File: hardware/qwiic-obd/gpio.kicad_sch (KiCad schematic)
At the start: 24 parts, among them SW401 SW_Push, U401 TCA9534, U402 MCP3423, U403 TCA9534, U404 ADM6320BX33ARJZ-R7, U405 TCA9534

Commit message: Added initial layout (parts dump)
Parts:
- C402: value 100uF 6V3 -> 10uF 6V3; footprint (none) -> Capacitor_SMD:C_0805_2012Metric_Pad1.18x1.45mm_HandSolder
- D401, D403: footprint Diode_SMD:D_0402_1005Metric_Pad0.77x0.64mm_HandSolder -> Diode_SMD:D_SOD-523
- R409: footprint (none) -> Resistor_SMD:R_0805_2012Metric_Pad1.20x1.40mm_HandSolder
- RN401, RN402, RN403: footprint Package_SO:SOIC-16_3.9x9.9mm_P1.27mm -> UltraLibrarian:742C163103JP
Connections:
- net +3V3_NOSW: now also RN402.7 (R7.1)
- net CAN_SOF: now also RN402.9 (R8.2), U403.12 (P7); no longer RN402.10 (R7.2), U403.11 (P6)
- net GND: no longer RN402.7 (R7.1)
- net ~{CAN_RESET}: no longer names the net of RN402.11 (R6.2), U403.10 (P5)
- new net: RN402.10 (R7.2), U403.11 (P6)
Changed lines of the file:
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@@
   (junction (at 106.68 48.26) (diameter 0) (color 0 0 0 0)
   )
-  (junction (at 106.68 115.57) (diameter 0) (color 0 0 0 0)
-  )
   (junction (at 96.52 83.82) (diameter 0) (color 0 0 0 0)
   )
@@
   (junction (at 99.06 107.95) (diameter 0) (color 0 0 0 0)
   )
+  (junction (at 109.22 118.11) (diameter 0) (color 0 0 0 0)
+  )
   (junction (at 101.6 67.31) (diameter 0) (color 0 0 0 0)
   )
@@
   (junction (at 62.23 173.99) (diameter 0) (color 0 0 0 0)
   )
+  (junction (at 104.14 83.82) (diameter 0) (color 0 0 0 0)
+  )
   (junction (at 148.59 83.82) (diameter 0) (color 0 0 0 0)
   )
@@
   (junction (at 74.93 59.69) (diameter 0) (color 0 0 0 0)
   )
-  (junction (at 104.14 113.03) (diameter 0) (color 0 0 0 0)
-  )
   (junction (at 101.6 83.82) (diameter 0) (color 0 0 0 0)
   )
@@
   )
   (junction (at 109.22 67.31) (diameter 0) (color 0 0 0 0)
-  )
-  (junction (at 109.22 81.28) (diameter 0) (color 0 0 0 0)
   )
   (junction (at 55.88 142.24) (diameter 0) (color 0 0 0 0)
@@
     (stroke (width 0) (type default) (color 0 0 0 0))
   )
-  (wire (pts (xy 106.68 115.57) (xy 111.76 115.57))
-    (stroke (width 0) (type default) (color 0 0 0 0))
-  )
   (wire (pts (xy 106.68 139.7) (xy 109.22 139.7))
     (stroke (width 0) (type default) (color 0 0 0 0))
@@
     (stroke (width 0) (type default) (color 0 0 0 0))
   )
-  (wire (pts (xy 106.68 81.28) (xy 109.22 81.28))
-    (stroke (width 0) (type default) (color 0 0 0 0))
-  )
   (wire (pts (xy 63.5 142.24) (xy 63.5 171.45))
     (stroke (width 0) (type default) (color 0 0 0 0))
@@
     (stroke (width 0) (type default) (color 0 0 0 0))
   )
+  (wire (pts (xy 106.68 83.82) (xy 104.14 83.82))
+    (stroke (width 0) (type default) (color 0 0 0 0))
+  )
   (wire (pts (xy 55.88 142.24) (xy 63.5 142.24))
     (stroke (width 0) (type default) (color 0 0 0 0))
@@
     (stroke (width 0) (type default) (color 0 0 0 0))
   )
+  (wire (pts (xy 109.22 118.11) (xy 111.76 118.11))
+    (stroke (width 0) (type default) (color 0 0 0 0))
+  )
   (wire (pts (xy 104.14 139.7) (xy 104.14 143.51))
     (stroke (width 0) (type default) (color 0 0 0 0))
@@
     (stroke (width 0) (type default) (color 0 0 0 0))
   )
+  (wire (pts (xy 106.68 87.63) (xy 106.68 83.82))
+    (stroke (width 0) (type default) (color 0 0 0 0))
+  )
   (wire (pts (xy 205.74 64.77) (xy 220.98 64.77))
     (stroke (width 0) (type default) (color 0 0 0 0))
@@
     (stroke (width 0) (type default) (color 0 0 0 0))
   )
-  (wire (pts (xy 104.14 113.03) (xy 111.76 113.03))
-    (stroke (width 0) (type default) (color 0 0 0 0))
-  )
   (wire (pts (xy 186.69 132.08) (xy 190.5 132.08))
     (stroke (width 0) (type default) (color 0 0 0 0))
@@
   )
   (wire (pts (xy 109.22 67.31) (xy 109.22 71.12))
-    (stroke (width 0) (type default) (color 0 0 0 0))
-  )
-  (wire (pts (xy 106.68 87.63) (xy 106.68 81.28))
     (stroke (width 0) (type default) (color 0 0 0 0))
   )
@@
     )
   )
-  (global_label "CAN_SOF" (shape input) (at 111.76 115.57 0) (fields_autoplaced)
+  (global_label "CAN_SOF" (shape input) (at 111.76 118.11 0) (fields_autoplaced)
     (effects (font (size 1.27 1.27)) (justify left))
-    (property "Intersheet References" "${INTERSHEET_REFS}" (id 0) (at 122.4583 115.4906 0)
+    (property "Intersheet References" "${INTERSHEET_REFS}" (id 0) (at 122.4583 118.0306 0)
       (effects (font (size 1.27 1.27)) (justify left) hide)
     )
@@
     (property "Intersheet References" "${INTERSHEET_REFS}" (id 0) (at 126.4734 43.1118 0)
       (effects (font (size 1.0922 1.0922)) (justify left) hide)
-    )
-  )
-  (global_label "~{CAN_RESET}" (shape output) (at 111.76 113.03 0) (fields_autoplaced)
-    (effects (font (size 1.27 1.27)) (justify left))
-    (property "Intersheet References" "${INTERSHEET_REFS}" (id 0) (at 124.575 112.9506 0)
-      (effects (font (size 1.27 1.27)) (justify left) hide)
     )
   )
@@
       (effects (font (size 1.27 1.27)) (justify left))
     )
-    (property "Footprint" "Package_SO:SOIC-16_3.9x9.9mm_P1.27mm" (id 2) (at 113.665 92.71 90)
+    (property "Footprint" "UltraLibrarian:742C163103JP" (id 2) (at 113.665 92.71 90)
       (effects (font (size 1.27 1.27)) hide)
     )
@@
       (effects (font (size 1.27 1.27)) (justify left))
     )
-    (property "Footprint" "Diode_SMD:D_0402_1005Metric_Pad0.77x0.64mm_HandSolder" (id 2) (at 180.34 52.07 0)
+    (property "Footprint" "Diode_SMD:D_SOD-523" (id 2) (at 180.34 52.07 0)
       (effects (font (size 1.27 1.27)) hide)
     )
@@
       (effects (font (size 1.27 1.27)) (justify left))
     )
-    (property "Footprint" "Package_SO:SOIC-16_3.9x9.9mm_P1.27mm" (id 2) (at 113.665 58.42 90)
+    (property "Footprint" "UltraLibrarian:742C163103JP" (id 2) (at 113.665 58.42 90)
       (effects (font (size 1.27 1.27)) hide)
     )
@@
       (effects (font (size 1.27 1.27)) (justify left))
     )
-    (property "Footprint" "" (id 2) (at 54.102 149.86 90)
+    (property "Footprint" "Resistor_SMD:R_0805_2012Metric_Pad1.20x1.40mm_HandSolder" (id 2) (at 54.102 149.86 90)
       (effects (font (size 1.27 1.27)) hide)
     )
@@
       (effects (font (size 1.27 1.27)) (justify left))
     )
-    (property "Footprint" "Diode_SMD:D_0402_1005Metric_Pad0.77x0.64mm_HandSolder" (id 2) (at 179.07 88.9 0)
+    (property "Footprint" "Diode_SMD:D_SOD-523" (id 2) (at 179.07 88.9 0)
       (effects (font (size 1.27 1.27)) hide)
     )
@@
       (effects (font (size 1.27 1.27)) (justify right))
     )
-    (property "Value" "100uF 6V3" (id 1) (at 138.43 90.1699 0)
+    (property "Value" "10uF 6V3" (id 1) (at 138.43 90.1699 0)
       (effects (font (size 1.27 1.27)) (justify right))
     )
-    (property "Footprint" "" (id 2) (at 143.2052 85.09 0)
+    (property "Footprint" "Capacitor_SMD:C_0805_2012Metric_Pad1.18x1.45mm_HandSolder" (id 2) (at 143.2052 85.09 0)
       (effects (font (size 1.27 1.27)) hide)
     )
@@
       (effects (font (size 1.27 1.27)) (justify left))
     )
-    (property "Footprint" "Package_SO:SOIC-16_3.9x9.9mm_P1.27mm" (id 2) (at 113.665 148.59 90)
-      (effects (font (size 1.27 1.27)) hide)
-    )
+    (property "Footprint" "UltraLibrarian:742C163103JP" (id 2) (at 113.665 148.59 90)
+      (effects (font (size 1.27 1.27)) hide)
+    )

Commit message: OK, layout v1 complete
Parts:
- removed R409: 10k, Resistor_SMD:R_0805_2012Metric_Pad1.20x1.40mm_HandSolder, symbol Device:R
- removed RN403: 10k, UltraLibrarian:742C163103JP, symbol Device:R_Pack08
- removed U405: TCA9534, Package_SO:TSSOP-16_4.4x5mm_P0.65mm, symbol Interface_Expansion:TCA9534
- added J401: 1x4, Connector_PinSocket_2.54mm:PinSocket_1x04_P2.54mm_Vertical, symbol SparkFun-Connectors:M04JST-PTH
- added RN403: 10k, Resistor_THT:R_Array_SIP5, symbol Device:R_Network04
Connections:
- net +3V3_NOSW: now also RN402.10 (R7.2), RN402.11 (R6.2), RN402.12 (R5.2), RN402.13 (R4.2), RN402.14 (R3.2), RN402.15 (R2.2), RN402.16 (R1.2), RN403.1 (common); no longer RN402.1 (R1.1), RN402.2 (R2.1), RN402.3 (R3.1), RN402.4 (R4.1), RN402.5 (R5.1), RN402.6 (R6.1), RN402.7 (R7.1)
- net CAN_SOF: now also RN402.8 (R8.1); no longer RN402.9 (R8.2)
- net GND: now also RN402.9 (R8.2); no longer RN402.8 (R8.1)
- net ~{CAN_INT}: now also J401.1, RN403.2 (R1)
- net ~{CAN_RX0BF}: now also RN402.1 (R1.1); no longer RN402.16 (R1.2)
- net ~{CAN_RX1BF}: now also RN402.2 (R2.1); no longer RN402.15 (R2.2)
- net ~{CAN_TX0RTS}: now also RN402.3 (R3.1); no longer RN402.14 (R3.2)
- net ~{CAN_TX1RTS}: now also RN402.4 (R4.1); no longer RN402.13 (R4.2)
- net ~{CAN_TX2RTS}: now also RN402.5 (R5.1); no longer RN402.12 (R5.2)
- net ~{J1850_INT}: now also J401.4, RN403.5 (R4)
- net ~{RESET}: now also RN402.7 (R7.1), U403.11 (P6)
- net ~{SPI_INT}: now also J401.3, RN403.4 (R3)
- net ~{UART_INT}: now also J401.2, RN403.3 (R2)
- net at U403.10 (P5): now also RN402.6 (R6.1); no longer RN402.11 (R6.2)
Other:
- note removed: "I2C Address 0x22"
- moved on the sheet: RN402

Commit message: Fix title block
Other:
- title: (none) -> QWIIC OBDII Interface
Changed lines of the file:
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@@
 (kicad_sch (version 20211123) (generator eeschema)
   (paper "A4")
+  (title_block
+    (title "QWIIC OBDII Interface")
+    (date "2023-01-03")
+  )
   (junction (at 236.22 76.2) (diameter 0) (color 0 0 0 0)
   )

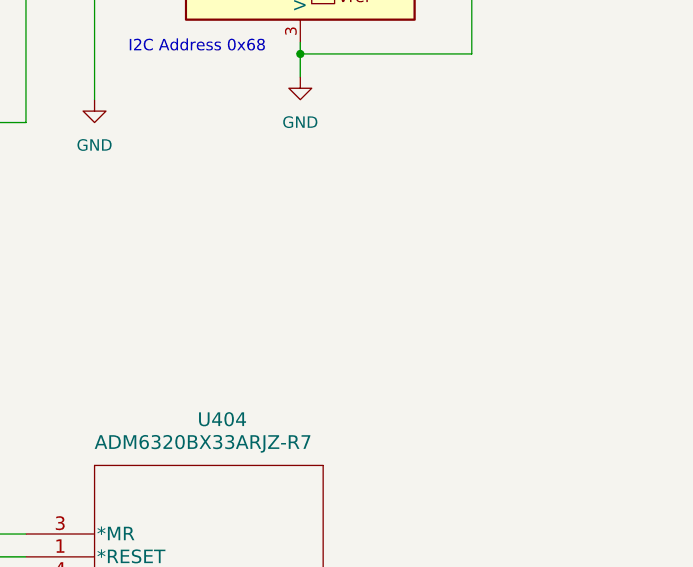
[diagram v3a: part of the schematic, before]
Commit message: Add PIC bootloader, update silkscreen
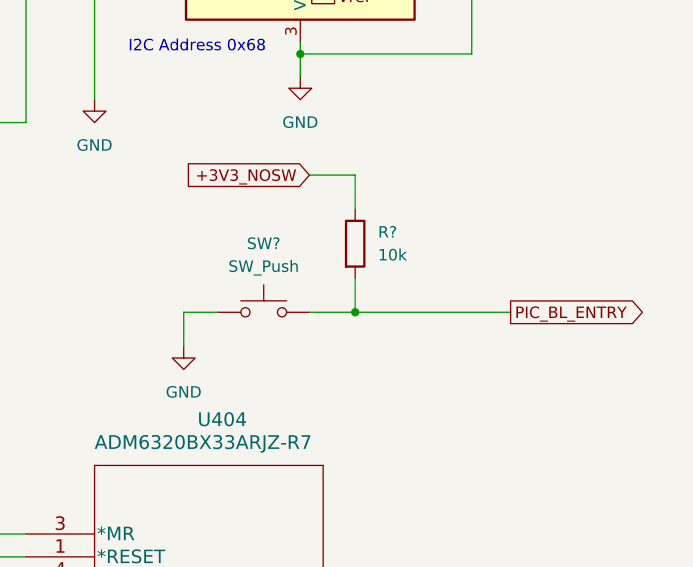
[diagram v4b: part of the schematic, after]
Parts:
- added R?: 10k, Resistor_SMD:R_0805_2012Metric_Pad1.20x1.40mm_HandSolder, symbol Device:R
- added SW?: SW_Push, Button_Switch_THT:SW_PUSH_6mm, symbol Switch:SW_Push
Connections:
- net +3V3_NOSW: now also R?.1
- net GND: now also SW?.1
- new net PIC_BL_ENTRY: R?.2, SW?.2
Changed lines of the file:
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@@
   (junction (at 167.64 46.99) (diameter 0) (color 0 0 0 0)
+  )
+  (junction (at 242.316 104.902) (diameter 0) (color 0 0 0 0)
   )
   (junction (at 101.6 137.16) (diameter 0) (color 0 0 0 0)
@@
     (stroke (width 0) (type default) (color 0 0 0 0))
   )
+  (wire (pts (xy 223.266 108.712) (xy 223.266 104.902))
+    (stroke (width 0) (type default) (color 0 0 0 0))
+  )
   (wire (pts (xy 109.22 132.08) (xy 109.22 137.16))
     (stroke (width 0) (type default) (color 0 0 0 0))
@@
     (stroke (width 0) (type default) (color 0 0 0 0))
   )
+  (wire (pts (xy 223.266 104.902) (xy 227.076 104.902))
+    (stroke (width 0) (type default) (color 0 0 0 0))
+  )
   (wire (pts (xy 93.98 67.31) (xy 96.52 67.31))
     (stroke (width 0) (type default) (color 0 0 0 0))
@@
     (stroke (width 0) (type default) (color 0 0 0 0))
   )
+  (wire (pts (xy 242.316 104.902) (xy 259.588 104.902))
+    (stroke (width 0) (type default) (color 0 0 0 0))
+  )
   (wire (pts (xy 255.27 67.31) (xy 255.27 76.2))
     (stroke (width 0) (type default) (color 0 0 0 0))
@@
     (stroke (width 0) (type default) (color 0 0 0 0))
   )
+  (wire (pts (xy 242.316 89.662) (xy 242.316 93.472))
+    (stroke (width 0) (type default) (color 0 0 0 0))
+  )
   (wire (pts (xy 106.68 115.57) (xy 111.76 115.57))
     (stroke (width 0) (type default) (color 0 0 0 0))
@@
     (stroke (width 0) (type default) (color 0 0 0 0))
   )
+  (wire (pts (xy 237.236 89.662) (xy 242.316 89.662))
+    (stroke (width 0) (type default) (color 0 0 0 0))
+  )
   (wire (pts (xy 109.22 63.5) (xy 109.22 67.31))
     (stroke (width 0) (type default) (color 0 0 0 0))
@@
     (stroke (width 0) (type default) (color 0 0 0 0))
   )
+  (wire (pts (xy 242.316 104.902) (xy 242.316 101.092))
+    (stroke (width 0) (type default) (color 0 0 0 0))
+  )
   (wire (pts (xy 167.64 44.704) (xy 167.64 46.99))
     (stroke (width 0) (type default) (color 0 0 0 0))
@@
   )
   (wire (pts (xy 85.09 50.8) (xy 109.22 50.8))
+    (stroke (width 0) (type default) (color 0 0 0 0))
+  )
+  (wire (pts (xy 237.236 104.902) (xy 242.316 104.902))
     (stroke (width 0) (type default) (color 0 0 0 0))
   )
@@
     )
   )
+  (global_label "PIC_BL_ENTRY" (shape output) (at 259.588 104.902 0) (fields_autoplaced)
+    (effects (font (size 1.27 1.27)) (justify left))
+    (property "Intersheet References" "${INTERSHEET_REFS}" (id 0) (at 275.1849 104.8226 0)
+      (effects (font (size 1.27 1.27)) (justify left) hide)
+    )
+  )
   (global_label "CAN_SEL0" (shape output) (at 111.76 50.8 0) (fields_autoplaced)
     (effects (font (size 1.27 1.27)) (justify left))
     (property "Intersheet References" "${INTERSHEET_REFS}" (id 0) (at 123.426 50.7206 0)
       (effects (font (size 1.27 1.27)) (justify left) hide)
+    )
+  )
+  (global_label "+3V3_NOSW" (shape input) (at 237.236 89.662 180) (fields_autoplaced)
+    (effects (font (size 1.27 1.27)) (justify right))
+    (property "Intersheet References" "${INTERSHEET_REFS}" (id 0) (at 223.4534 89.5826 0)
+      (effects (font (size 1.27 1.27)) (justify right) hide)
     )
   )
@@
     (pin "2")
   )
+  (symbol (lib_id "power:GND") (at 223.266 108.712 0) (unit 1)
+    (in_bom yes) (on_board yes) (fields_autoplaced)
+    (property "Reference" "#PWR?" (id 0) (at 223.266 115.062 0)
+      (effects (font (size 1.27 1.27)) hide)
+    )
+    (property "Value" "GND" (id 1) (at 223.266 113.792 0))
+    (property "Footprint" "" (id 2) (at 223.266 108.712 0)
+      (effects (font (size 1.27 1.27)) hide)
+    )
+    (property "Datasheet" "" (id 3) (at 223.266 108.712 0)
+      (effects (font (size 1.27 1.27)) hide)
+    )
+    (pin "1")
+  )
   (symbol (lib_id "Interface_Expansion:TCA9534") (at 74.93 107.95 0) (unit 1)
     (in_bom yes) (on_board yes) (fields_autoplaced)
@@
     (pin "1")
   )
+  (symbol (lib_id "Device:R") (at 242.316 97.282 0) (unit 1)
+    (in_bom yes) (on_board yes) (fields_autoplaced)
+    (property "Reference" "R?" (id 0) (at 244.856 96.0119 0)
+      (effects (font (size 1.27 1.27)) (justify left))
+    )
+    (property "Value" "10k" (id 1) (at 244.856 98.5519 0)
+      (effects (font (size 1.27 1.27)) (justify left))
+    )
+    (property "Footprint" "Resistor_SMD:R_0805_2012Metric_Pad1.20x1.40mm_HandSolder" (id 2) (at 240.538 97.282 90)
+      (effects (font (size 1.27 1.27)) hide)
+    )
+    (property "Datasheet" "~" (id 3) (at 242.316 97.282 0)
+      (effects (font (size 1.27 1.27)) hide)
+    )
+    (pin "1")
+    (pin "2")
+  )
   (symbol (lib_id "Device:R") (at 180.34 121.92 0) (unit 1)
     (in_bom yes) (on_board yes) (fields_autoplaced)
@@
     (pin "1")
   )
+  (symbol (lib_id "Switch:SW_Push") (at 232.156 104.902 0) (unit 1)
+    (in_bom yes) (on_board yes) (fields_autoplaced)
+    (property "Reference" "SW?" (id 0) (at 232.156 97.282 0))
+    (property "Value" "SW_Push" (id 1) (at 232.156 99.822 0))
+    (property "Footprint" "Button_Switch_THT:SW_PUSH_6mm" (id 2) (at 232.156 99.822 0)
+      (effects (font (size 1.27 1.27)) hide)
+    )
+    (property "Datasheet" "~" (id 3) (at 232.156 99.822 0)
+      (effects (font (size 1.27 1.27)) hide)
+    )
+    (pin "1")
+    (pin "2")
+  )
   (symbol (lib_id "power:+3V3") (at 236.22 48.26 0) (unit 1)

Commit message: Split firmware into two separate projects
- got it building into different parts of the FLASH.
- bootloader - 0x000 - 0x3FF (word addresses)
- application - 0x400 - end  (word addresses)
- reset vector and interrupt vector are also mirrored
  into 0x400 and 0x404 (respectively) for application
  use, and are linked to from the bootloader
- when the BL_ENABLE button is pushed while in the
  application, a falling edge interrupt causes a reset
  back into the bootloader.
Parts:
- gave numbers to parts that had none: 2
- renumbered R407 to R408, R408 to R409, SW401 to SW402
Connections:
- net PIC_BL_ENTRY renamed ~{PIC_BL_ENTRY}
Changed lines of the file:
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@@
     )
   )
-  (global_label "PIC_BL_ENTRY" (shape output) (at 259.588 104.902 0) (fields_autoplaced)
+  (global_label "~{PIC_BL_ENTRY}" (shape output) (at 259.588 104.902 0) (fields_autoplaced)
     (effects (font (size 1.27 1.27)) (justify left))
     (property "Intersheet References" "${INTERSHEET_REFS}" (id 0) (at 275.1849 104.8226 0)
@@
   (symbol (lib_id "Device:R") (at 190.5 121.92 0) (unit 1)
     (in_bom yes) (on_board yes) (fields_autoplaced)
-    (property "Reference" "R408" (id 0) (at 193.04 120.6499 0)
+    (property "Reference" "R409" (id 0) (at 193.04 120.6499 0)
       (effects (font (size 1.27 1.27)) (justify left))
     )
@@
   (symbol (lib_id "Switch:SW_Push") (at 170.18 129.54 0) (unit 1)
     (in_bom yes) (on_board yes) (fields_autoplaced)
-    (property "Reference" "SW401" (id 0) (at 170.18 121.92 0))
+    (property "Reference" "SW402" (id 0) (at 170.18 121.92 0))
     (property "Value" "SW_Push" (id 1) (at 170.18 124.46 0))
     (property "Footprint" "Button_Switch_THT:SW_PUSH_6mm" (id 2) (at 170.18 124.46 0)
@@
   (symbol (lib_id "power:GND") (at 199.39 152.4 0) (unit 1)
     (in_bom yes) (on_board yes) (fields_autoplaced)
-    (property "Reference" "#PWR0411" (id 0) (at 199.39 158.75 0)
+    (property "Reference" "#PWR0412" (id 0) (at 199.39 158.75 0)
       (effects (font (size 1.27 1.27)) hide)
     )
@@
   (symbol (lib_id "power:GND") (at 223.266 108.712 0) (unit 1)
     (in_bom yes) (on_board yes) (fields_autoplaced)
-    (property "Reference" "#PWR?" (id 0) (at 223.266 115.062 0)
+    (property "Reference" "#PWR0408" (id 0) (at 223.266 115.062 0)
       (effects (font (size 1.27 1.27)) hide)
     )
@@
   (symbol (lib_id "power:GND") (at 161.29 133.35 0) (unit 1)
     (in_bom yes) (on_board yes) (fields_autoplaced)
-    (property "Reference" "#PWR0409" (id 0) (at 161.29 139.7 0)
+    (property "Reference" "#PWR0410" (id 0) (at 161.29 139.7 0)
       (effects (font (size 1.27 1.27)) hide)
     )
@@
   (symbol (lib_id "Device:R") (at 242.316 97.282 0) (unit 1)
     (in_bom yes) (on_board yes) (fields_autoplaced)
-    (property "Reference" "R?" (id 0) (at 244.856 96.0119 0)
+    (property "Reference" "R407" (id 0) (at 244.856 96.0119 0)
       (effects (font (size 1.27 1.27)) (justify left))
     )
@@
   (symbol (lib_id "Device:R") (at 180.34 121.92 0) (unit 1)
     (in_bom yes) (on_board yes) (fields_autoplaced)
-    (property "Reference" "R407" (id 0) (at 182.88 120.6499 0)
+    (property "Reference" "R408" (id 0) (at 182.88 120.6499 0)
       (effects (font (size 1.27 1.27)) (justify left))
     )
@@
   (symbol (lib_id "power:GND") (at 74.93 128.27 0) (unit 1)
     (in_bom yes) (on_board yes) (fields_autoplaced)
-    (property "Reference" "#PWR0408" (id 0) (at 74.93 134.62 0)
+    (property "Reference" "#PWR0409" (id 0) (at 74.93 134.62 0)
       (effects (font (size 1.27 1.27)) hide)
     )
@@
   (symbol (lib_id "power:GND") (at 109.22 137.16 0) (unit 1)
     (in_bom yes) (on_board yes) (fields_autoplaced)
-    (property "Reference" "#PWR0410" (id 0) (at 109.22 143.51 0)
+    (property "Reference" "#PWR0411" (id 0) (at 109.22 143.51 0)
       (effects (font (size 1.27 1.27)) hide)
     )
@@
   (symbol (lib_id "Switch:SW_Push") (at 232.156 104.902 0) (unit 1)
     (in_bom yes) (on_board yes) (fields_autoplaced)
-    (property "Reference" "SW?" (id 0) (at 232.156 97.282 0))
+    (property "Reference" "SW401" (id 0) (at 232.156 97.282 0))
     (property "Value" "SW_Push" (id 1) (at 232.156 99.822 0))
     (property "Footprint" "Button_Switch_THT:SW_PUSH_6mm" (id 2) (at 232.156 99.822 0)

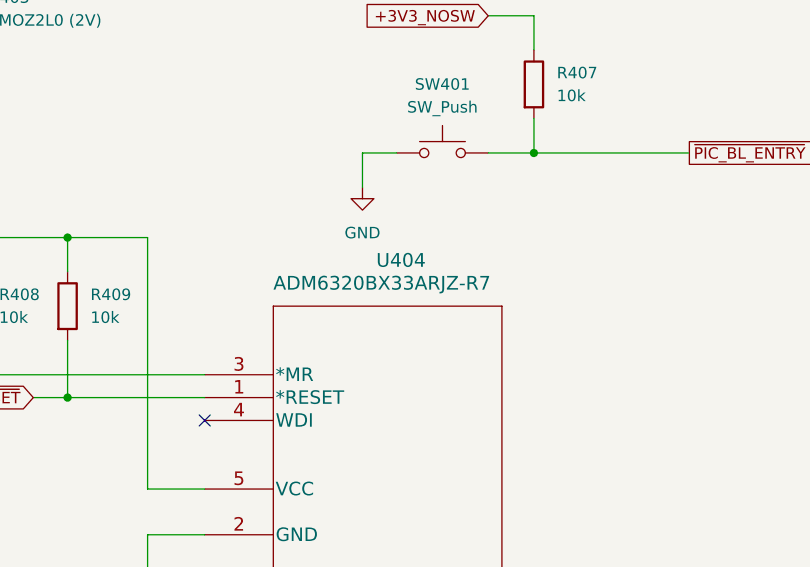
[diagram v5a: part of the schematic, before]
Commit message: Shrunk layout a bit
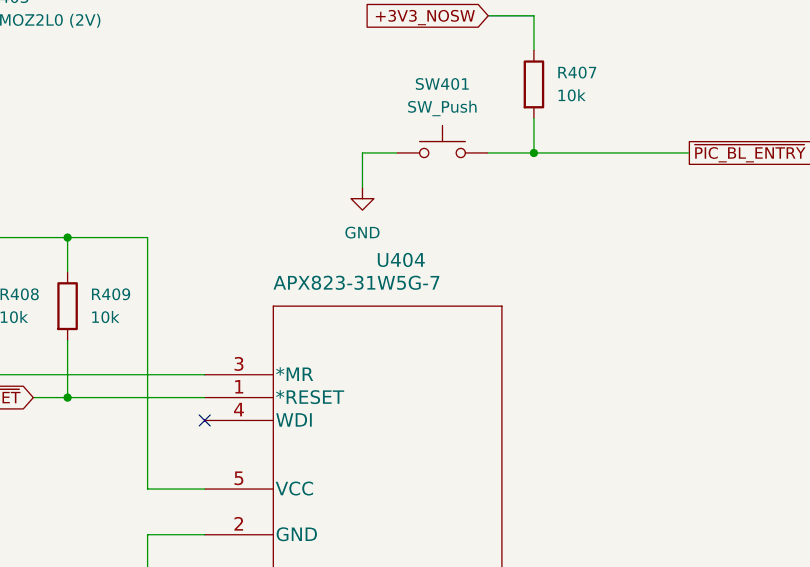
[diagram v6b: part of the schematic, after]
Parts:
- U404: value ADM6320BX33ARJZ-R7 -> APX823-31W5G-7
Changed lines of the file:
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@@
       (effects (font (size 1.524 1.524)) (justify left))
     )
-    (property "Value" "ADM6320BX33ARJZ-R7" (id 1) (at 213.36 119.38 0)
+    (property "Value" "APX823-31W5G-7" (id 1) (at 213.36 119.38 0)
       (effects (font (size 1.524 1.524)) (justify left))
     )
